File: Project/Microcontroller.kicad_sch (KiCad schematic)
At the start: 22 parts, among them J701 Conn_01x05_Female, J702 Conn_01x04_Female, J703 Conn_01x04_Female, U701 STM32L031K6U3TR

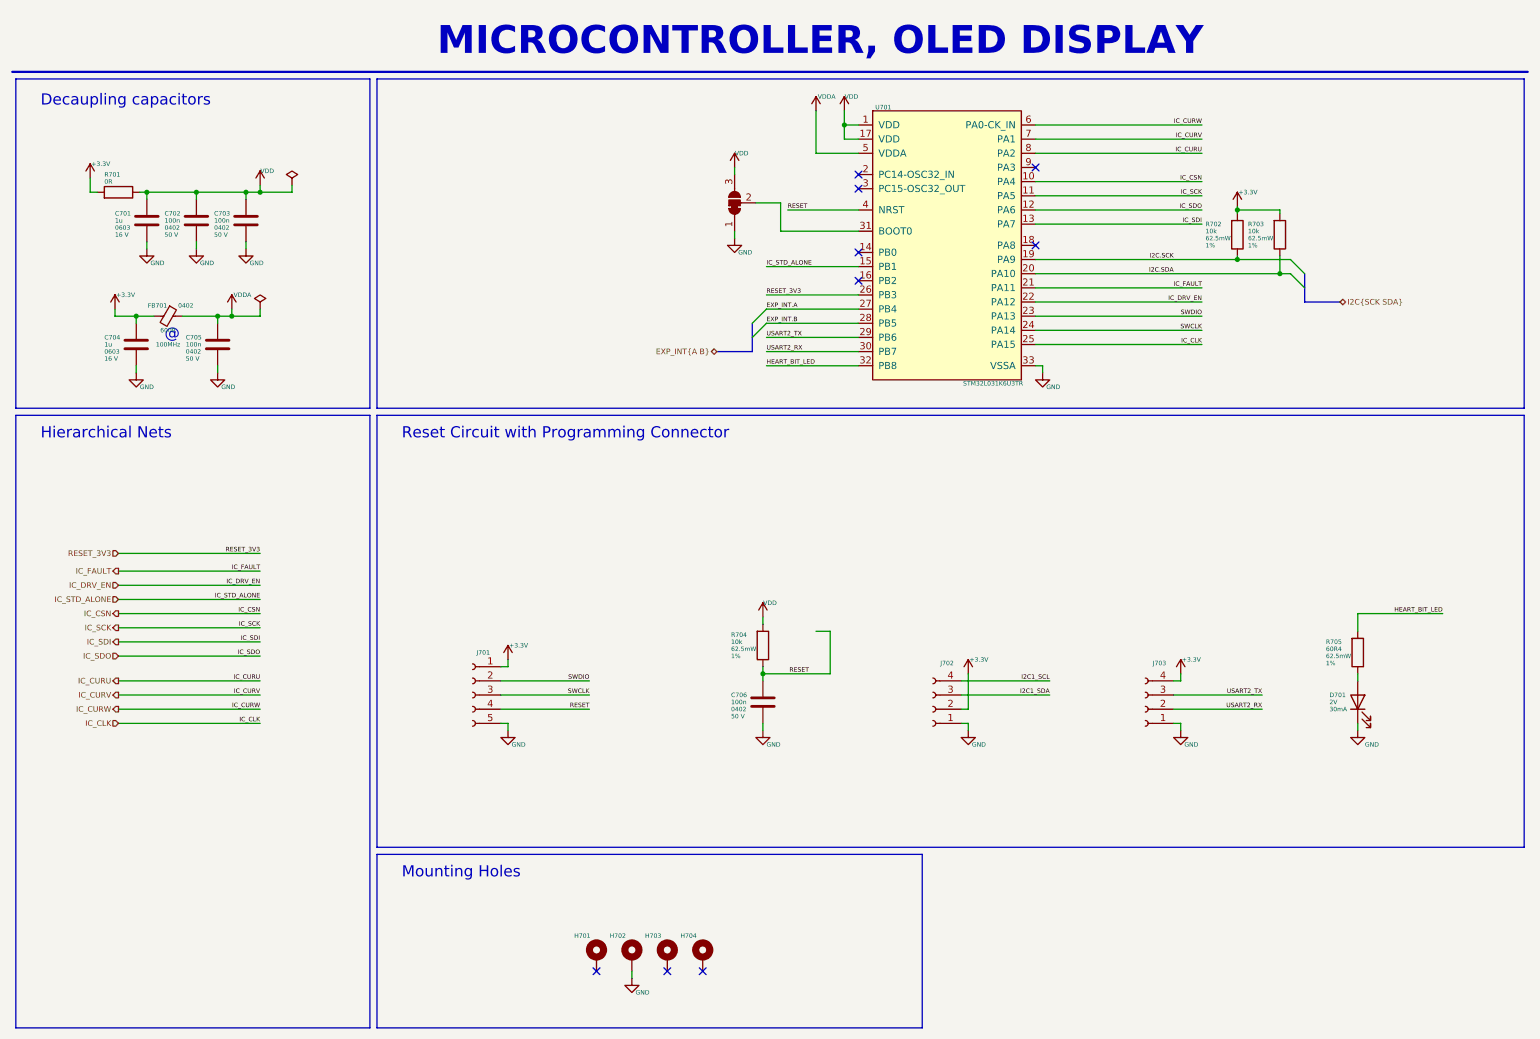
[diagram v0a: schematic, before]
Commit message: Cleaning files, added testpoints
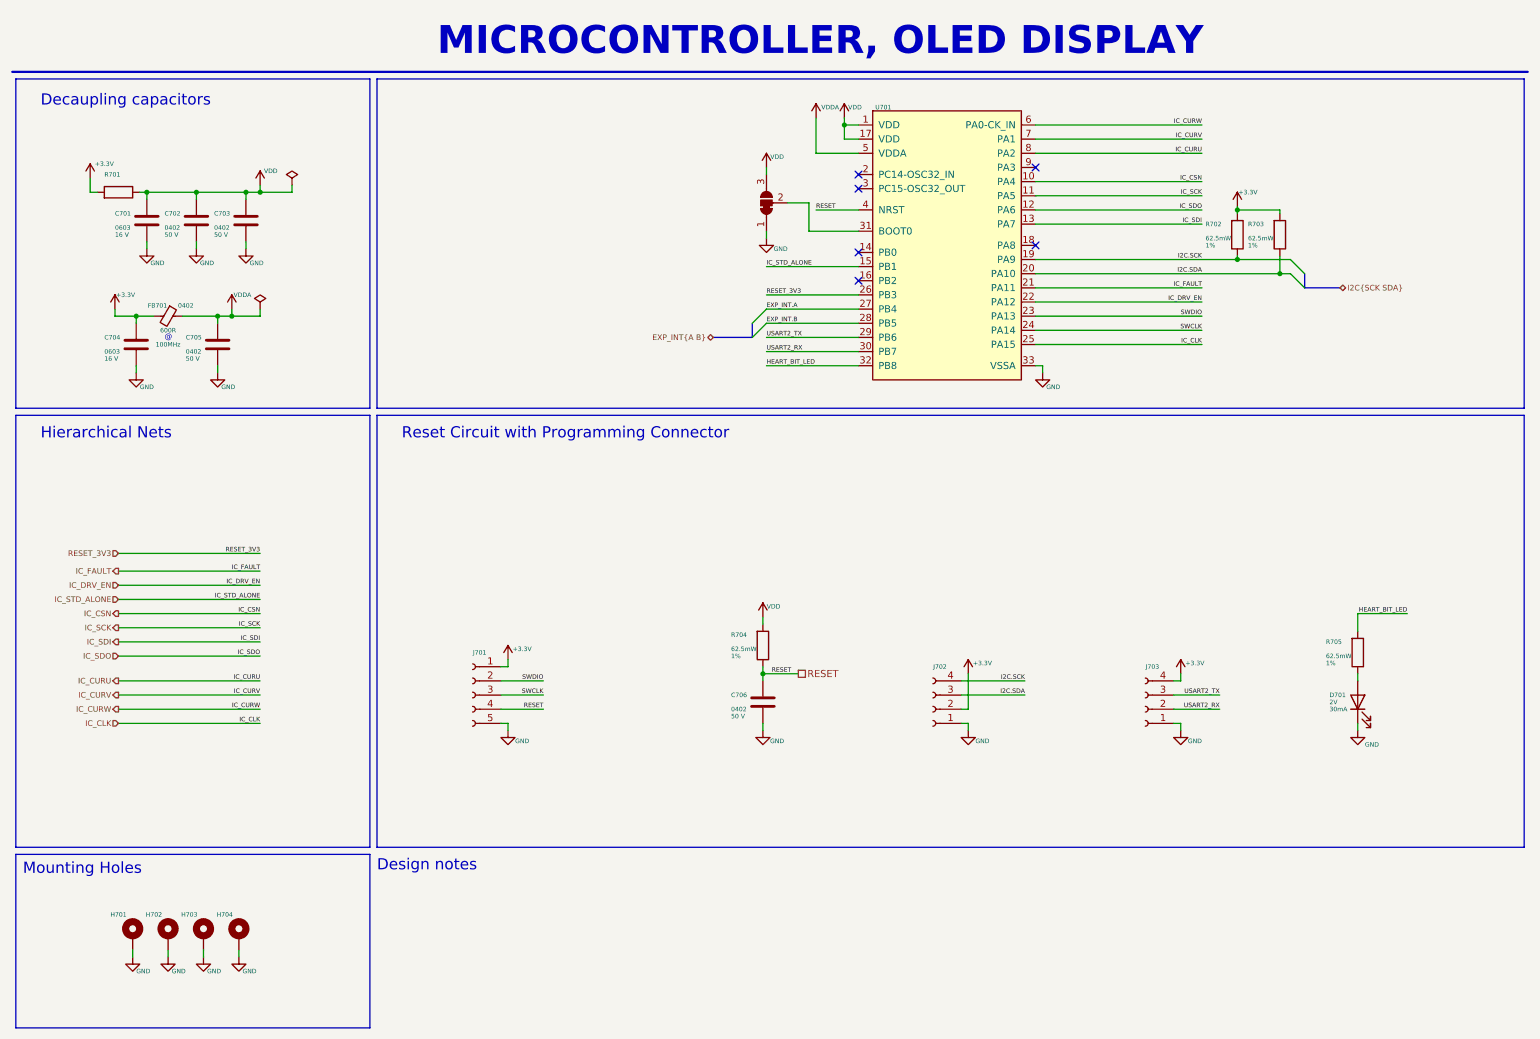
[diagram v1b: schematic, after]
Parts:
- C701, C704: value 1u -> (none); footprint Capacitor_SMD:C_0603_1608Metric -> (none)
- C702, C703, C705, C706: value 100n -> (none); footprint Capacitor_SMD:C_0402_1005Metric -> (none)
- D701: value LED -> (none); footprint Diode_SMD:D_0402_1005Metric -> (none)
- FB701: value Ferrite_Bead -> (none); footprint Inductor_SMD:L_0402_1005Metric -> (none)
- H701, H702, H703, H704: value MountingHole_Pad -> (none); footprint MountingHole:MountingHole_2.7mm_M2.5_Pad_TopBottom -> (none)
- J701: value Conn_01x05_Female -> (none); footprint Connector_PinHeader_2.54mm:PinHeader_1x05_P2.54mm_Vertical -> (none)
- J702, J703: value Conn_01x04_Female -> (none); footprint Connector_PinHeader_2.54mm:PinHeader_1x04_P2.54mm_Vertical -> (none)
- JP701: value SolderJumper_3_Bridged12 -> (none); footprint Jumper:SolderJumper-3_P1.3mm_Bridged12_RoundedPad1.0x1.5mm_NumberLabels -> (none)
- R701: value 0R -> (none); footprint Resistor_SMD:R_0402_1005Metric -> (none)
- R702, R703, R704: value 10k -> (none); footprint Resistor_SMD:R_0402_1005Metric -> (none)
- R705: value 60R4 -> (none); footprint Resistor_SMD:R_0402_1005Metric -> (none)
- U701: value STM32L031K6U3TR -> (none); footprint FZ6N_GATEWAY:STM32L031K6U3TR_UFQFPN32 -> (none)
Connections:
- net I2C1_SCL is gone; now on net I2C.SCK: J702.4 (Pin_4)
- net I2C1_SDA is gone; now on net I2C.SDA: J702.3 (Pin_3)
- net GND: now also H701.1, H703.1, H704.1
- no-connect marks 9 -> 6
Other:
- note added: "Design notes"
- moved on the sheet: H701, H702, H703, H704
